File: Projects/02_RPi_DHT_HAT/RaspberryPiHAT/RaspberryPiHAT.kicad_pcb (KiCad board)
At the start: 2 copper layers, 27.4 x 20.6 mm, 9 parts, among them J1 Raspberry_Pi_2_3, SW1 SW_DPST, U1 DHT22

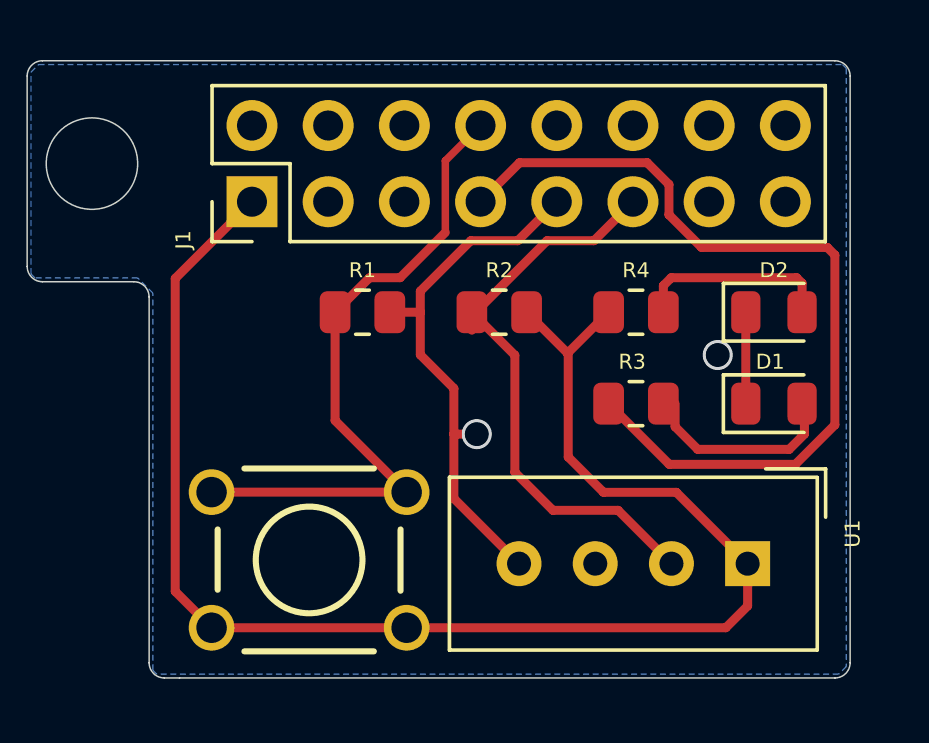
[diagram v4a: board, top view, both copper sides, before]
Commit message: Project 2: Add silkscreen text and graphics and generate gerber and drill files
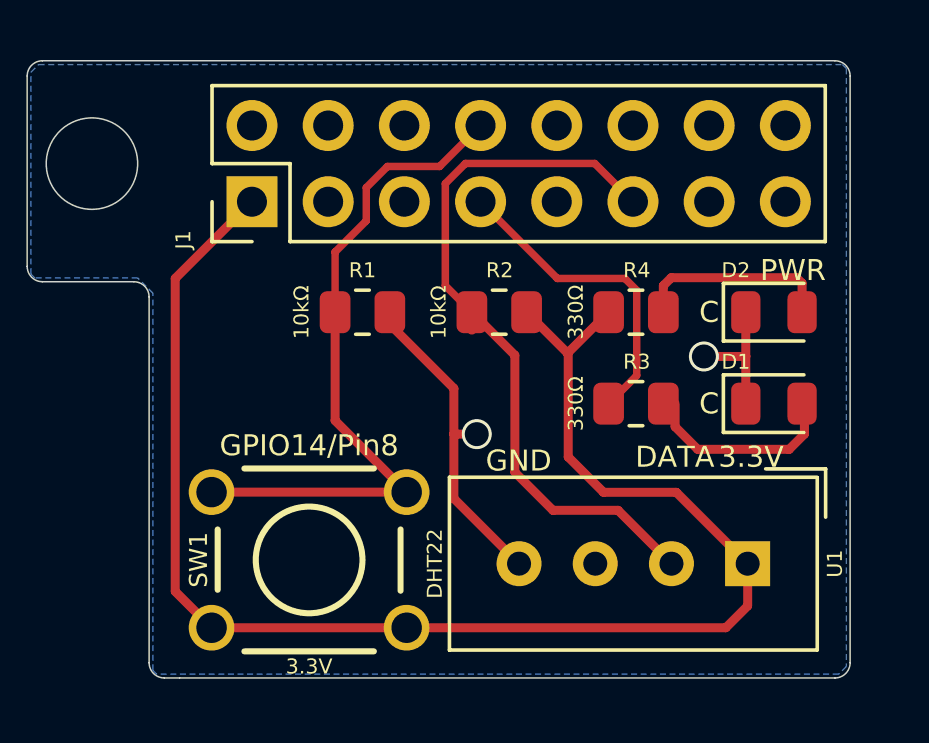
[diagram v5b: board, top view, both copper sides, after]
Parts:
- added REF**: OSHW-Logo2_7.3x6mm_SilkScreen, Symbol:OSHW-Logo2_7.3x6mm_SilkScreen, B.Cu at (207.0, 73.7)
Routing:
- net Net-(J1-Pad7): track 28.8 -> 10.6 mm
- net GND: track 21.1 -> 15.7 mm
- net Net-(J1-Pad11): track 20.3 -> 25.2 mm
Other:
- board text added: "10kΩ"
- board text added: "3.3V"
- board text added: "330Ω"
- board text added: "Button: GPIO14 LED: GPIO4"
- board text added: "C"
- board text added: "DATA"
- board text added: "DHT22"
- board text added: "Designed by Michael Ly github.com/Michael-Q-Ly"
- board text added: "GND"
- board text added: "GPIO14/Pin8"
- board text added: "PWR"
- board text added: "Raspberry Pi Full Stack Version 1"
